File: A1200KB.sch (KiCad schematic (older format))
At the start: 118 parts, among them J1 Conn_01x32_Female, K1 ESC, K10 F9, K11 F10, K12 TILDE, K13 1, K14 2, K15 3, K16 4, K17 5, K18 6, K19 7, K2 F1, K20 8, K21 9, K22 0, K23 MINUS, K24 PLUS, K25 PIPE, K26 BS, K27 DEL, K28 HELP, K29 NUM_(, K3 F2, K30 NUM_), K31 NUM_DIV, K32 NUM_MULT, K33 TAB, K34 Q, K35 W, K36 E, K37 R, K38 T, K39 Y, K4 F3, K40 U, K41 I, K42 O, K43 P, K44 L.CURLY, K45 R.CURLY, K46 RETURN, K47 NUM_7, K48 NUM_8, K49 NUM_9, K5 F4, K50 NUM_MINUS, K51 CTRL, K52 CAPSLOCK, K53 A, K54 S, K55 D, K56 F, K57 G, K58 H, K59 J, K6 F5, K60 K, K61 L, K62 COLON, K63 \", K64 R.BLANK, K65 UP, K66 NUM_4, K67 NUM_5, K68 NUM_6, K69 NUM_PLUS, K7 F6, K70 L.SHIFT, K71 L.BLANK, K72 Z, K73 X, K74 C, K75 V, K76 B, K77 N, K78 M, K79 R.CROC, K8 F7, K80 L.CROC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

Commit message: Added some global netlist
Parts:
- removed U1, U?: STM32F401-DK, RetroBitLab:STM32F401-DK, symbol AmigaComponents:STM32F401-DK
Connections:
- net 27: now also K98.1 (COL)
- net 3: no longer K98.1 (COL)
- no-connect marks 0 -> 1
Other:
- note added: "From LOCAL Nets to GLOBAL Nets"
- moved on the sheet: K98

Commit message: Updated from AEBERBACH GitHub repo
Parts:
- removed H1, H11, H12, H13, H14, H15, H17, H18, H19, H2, H3, H5, H6, H7, H8, H9: MountingHole_Pad, MountingHole:MountingHole_3mm_Pad, symbol Mechanical:MountingHole_Pad
- removed K97: MENU, RetroBitLab:SW_Cherry_MX1A_1.00u_PCB_3d, symbol AmigaComponents:MX-1U-MX_Alps_Hybrids
- removed K98: SUPER, RetroBitLab:SW_Cherry_MX1A_1.00u_PCB_3d, symbol AmigaComponents:MX-1U-MX_Alps_Hybrids
- removed K99: SPACE 9U, RetroBitLab:SW_Cherry_MX1A_9u_PCB_3d, symbol AmigaComponents:MX-7U-MX_Alps_Hybrids
- J1: footprint RetroBitLab:MOLEX-FFC-1.25mm-RA-52044-3245 -> Connector_FFC-FPC:FFC-1.25mm-RA-5204403245
- K1, K13, K14, K15, K16, K17, K18, K19, K20, K21, K22, K23, K24, K25, K26, K29, K30, K31, K32, K34, K35, K36, K37, K38, K39, K40, K41, K42, K43, K44, K45, K47, K48, K49, K50, K53, K54, K55, K56, K57, K58, K59, K60, K61, K62, K63, K64, K65, K66, K67, K68, K69, K71, K72, K73, K74, K75, K76, K77, K78, K79, K80, K81, K83, K84, K85, K86, K87, K88, K96: footprint RetroBitLab:SW_Cherry_MX1A_1.00u_PCB_3d -> MX_Alps_Hybrid:MXOnly-1U-NoLED; symbol AmigaComponents:MX-1U-MX_Alps_Hybrids -> A1200KB-rescue:MX-1U-MX_Alps_Hybrids
- K10, K11, K2, K3, K4, K5, K51, K6, K7, K8, K9, K90, K91, K93, K94: footprint RetroBitLab:SW_Cherry_MX1A_1.25u_PCB_3d -> MX_Alps_Hybrid:MXOnly-1.25U-NoLED; symbol AmigaComponents:MX-1.25U-MX_Alps_Hybrids -> A1200KB-rescue:MX-1.25U-MX_Alps_Hybrids
- K12, K27, K28: footprint RetroBitLab:SW_Cherry_MX1A_1.50u_PCB_3d -> MX_Alps_Hybrid:MXOnly-1.5U-NoLED; symbol AmigaComponents:MX-1.5U-MX_Alps_Hybrids -> A1200KB-rescue:MX-1.5U-MX_Alps_Hybrids
- K33: footprint RetroBitLab:SW_Cherry_MX1A_1.00u_PCB_3d -> MX_Alps_Hybrid:MXOnly-2U-NoLED; symbol AmigaComponents:MX-2U-MX_Alps_Hybrids -> A1200KB-rescue:MX-2U-MX_Alps_Hybrids
- K46: footprint RetroBitLab:SW_Cherry_MX1A_ISOEnter_Rotated_PCB_3d -> MX_Alps_Hybrid:MXOnly-ISO; symbol AmigaComponents:MX-ISO-MX_Alps_Hybrids -> A1200KB-rescue:MX-ISO-MX_Alps_Hybrids
- K52: footprint RetroBitLab:MXOnly-1U -> MX_Alps_Hybrid:MXOnly-1U; symbol AmigaComponents:MX-1U-MX_Alps_Hybrids -> A1200KB-rescue:MX-1U-MX_Alps_Hybrids
- K70: footprint RetroBitLab:SW_Cherry_MX1A_1.75u_PCB_3d -> MX_Alps_Hybrid:MXOnly-1.75U-NoLED; symbol AmigaComponents:MX-1.75U-MX_Alps_Hybrids -> A1200KB-rescue:MX-1.75U-MX_Alps_Hybrids
- K82: footprint RetroBitLab:SW_Cherry_MX1A_2.75u_PCB_3d -> MX_Alps_Hybrid:MXOnly-2.75U-NoLED; symbol AmigaComponents:MX-2.75U-MX_Alps_Hybrids -> A1200KB-rescue:MX-2.75U-MX_Alps_Hybrids
- K89: footprint RetroBitLab:SW_Cherry_MX1A_2.00u_Vertical_PCB_3d -> MX_Alps_Hybrid:MXOnly-2U-NoLED; symbol AmigaComponents:MX-2U-MX_Alps_Hybrids -> A1200KB-rescue:MX-2U-MX_Alps_Hybrids
- K92: value SPACE 7U -> SPACE; footprint RetroBitLab:MXOnly-7U-NoSwitch -> MX_Alps_Hybrid:MXOnly-7U-NoLED; symbol AmigaComponents:MX-7U-MX_Alps_Hybrids -> A1200KB-rescue:MX-7U-MX_Alps_Hybrids
- K95: footprint RetroBitLab:SW_Cherry_MX1A_2.00u_PCB_3d -> MX_Alps_Hybrid:MXOnly-2U-NoLED; symbol AmigaComponents:MX-2U-MX_Alps_Hybrids -> A1200KB-rescue:MX-2U-MX_Alps_Hybrids
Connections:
- net labels removed: CAPSLOCK_LED, COL1, COL10, COL11, COL12, COL13, COL14, COL15, COL2, COL3, COL4, COL5, COL6, COL7, COL8, COL9, GND, ROW1, ROW10, ROW11, ROW12, ROW13, ROW2, ROW3, ROW4, ROW5, ROW6, ROW7, ROW8, ROW9, VCC_5V
- wire segments 659 -> 568
- no-connect marks 1 -> 0
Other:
- note removed: "From LOCAL Nets to GLOBAL Nets"

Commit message: Now has the AmigaComponents.lib dependancy
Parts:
- added H1, H11, H12, H13, H14, H15, H16, H17, H18, H19, H2, H3, H5, H6, H7, H8, H9: MountingHole_Pad, MountingHole:MountingHole_3mm_Pad, symbol Mechanical:MountingHole_Pad
- added K97: MENU, RetroBitLab:SW_Cherry_MX1A_1.00u_PCB_3d, symbol AmigaComponents:MX-1U-MX_Alps_Hybrids
- added K98: SUPER, RetroBitLab:SW_Cherry_MX1A_1.00u_PCB_3d, symbol AmigaComponents:MX-1U-MX_Alps_Hybrids
- added K99: SPACE 9U, RetroBitLab:SW_Cherry_MX1A_9u_PCB_3d, symbol AmigaComponents:MX-7U-MX_Alps_Hybrids
- added U1: STM32F401-DK, RetroBitLab:STM32F401-DK, symbol AmigaComponents:STM32F401-DK
- J1: footprint Connector_FFC-FPC:FFC-1.25mm-RA-5204403245 -> RetroBitLab:MOLEX-FFC-1.25mm-RA-52044-3245
- K1, K13, K14, K15, K16, K17, K18, K19, K20, K21, K22, K23, K24, K25, K26, K29, K30, K31, K32, K34, K35, K36, K37, K38, K39, K40, K41, K42, K43, K44, K45, K47, K48, K49, K50, K53, K54, K55, K56, K57, K58, K59, K60, K61, K62, K63, K64, K65, K66, K67, K68, K69, K71, K72, K73, K74, K75, K76, K77, K78, K79, K80, K81, K83, K84, K85, K86, K87, K88, K96: footprint MX_Alps_Hybrid:MXOnly-1U-NoLED -> RetroBitLab:SW_Cherry_MX1A_1.00u_PCB_3d; symbol A1200KB-rescue:MX-1U-MX_Alps_Hybrids -> AmigaComponents:MX-1U-MX_Alps_Hybrids
- K10, K11, K2, K3, K4, K5, K51, K6, K7, K8, K9, K90, K91, K93, K94: footprint MX_Alps_Hybrid:MXOnly-1.25U-NoLED -> RetroBitLab:SW_Cherry_MX1A_1.25u_PCB_3d; symbol A1200KB-rescue:MX-1.25U-MX_Alps_Hybrids -> AmigaComponents:MX-1.25U-MX_Alps_Hybrids
- K12, K27, K28: footprint MX_Alps_Hybrid:MXOnly-1.5U-NoLED -> RetroBitLab:SW_Cherry_MX1A_1.50u_PCB_3d; symbol A1200KB-rescue:MX-1.5U-MX_Alps_Hybrids -> AmigaComponents:MX-1.5U-MX_Alps_Hybrids
- K33: footprint MX_Alps_Hybrid:MXOnly-2U-NoLED -> RetroBitLab:SW_Cherry_MX1A_1.00u_PCB_3d; symbol A1200KB-rescue:MX-2U-MX_Alps_Hybrids -> AmigaComponents:MX-2U-MX_Alps_Hybrids
- K46: footprint MX_Alps_Hybrid:MXOnly-ISO -> RetroBitLab:SW_Cherry_MX1A_ISOEnter_PCB_3d; symbol A1200KB-rescue:MX-ISO-MX_Alps_Hybrids -> AmigaComponents:MX-ISO-MX_Alps_Hybrids
- K52: footprint MX_Alps_Hybrid:MXOnly-1U -> RetroBitLab:MXOnly-1U; symbol A1200KB-rescue:MX-1U-MX_Alps_Hybrids -> AmigaComponents:MX-1U-MX_Alps_Hybrids
- K70: footprint MX_Alps_Hybrid:MXOnly-1.75U-NoLED -> RetroBitLab:SW_Cherry_MX1A_1.75u_PCB_3d; symbol A1200KB-rescue:MX-1.75U-MX_Alps_Hybrids -> AmigaComponents:MX-1.75U-MX_Alps_Hybrids
- K82: footprint MX_Alps_Hybrid:MXOnly-2.75U-NoLED -> RetroBitLab:SW_Cherry_MX1A_2.75u_PCB_3d; symbol A1200KB-rescue:MX-2.75U-MX_Alps_Hybrids -> AmigaComponents:MX-2.75U-MX_Alps_Hybrids
- K89: footprint MX_Alps_Hybrid:MXOnly-2U-NoLED -> RetroBitLab:SW_Cherry_MX1A_2.00u_Vertical_PCB_3d; symbol A1200KB-rescue:MX-2U-MX_Alps_Hybrids -> AmigaComponents:MX-2U-MX_Alps_Hybrids
- K92: value SPACE -> SPACE 7U; footprint MX_Alps_Hybrid:MXOnly-7U-NoLED -> RetroBitLab:MXOnly-7U-NoSwitch; symbol A1200KB-rescue:MX-7U-MX_Alps_Hybrids -> AmigaComponents:MX-7U-MX_Alps_Hybrids
- K95: footprint MX_Alps_Hybrid:MXOnly-2U-NoLED -> RetroBitLab:SW_Cherry_MX1A_2.00u_PCB_3d; symbol A1200KB-rescue:MX-2U-MX_Alps_Hybrids -> AmigaComponents:MX-2U-MX_Alps_Hybrids
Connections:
- net labels added: GND
- wire segments 568 -> 588

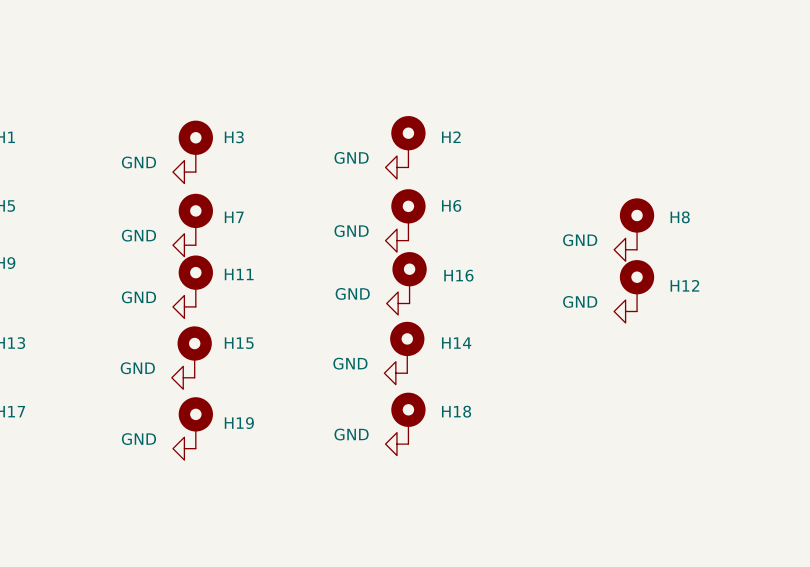
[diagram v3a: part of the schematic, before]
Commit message: The ISO Enter here, must have rotated Cherry MX switch by 180 degrees
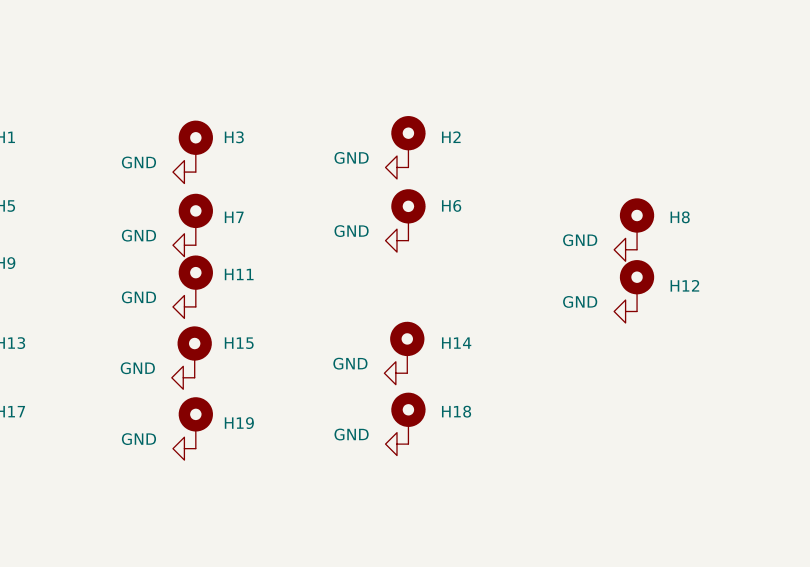
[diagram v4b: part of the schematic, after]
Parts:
- removed H16: MountingHole_Pad, MountingHole:MountingHole_3mm_Pad, symbol Mechanical:MountingHole_Pad
- K46: footprint RetroBitLab:SW_Cherry_MX1A_ISOEnter_PCB_3d -> RetroBitLab:SW_Cherry_MX1A_ISOEnter_Rotated_PCB_3d
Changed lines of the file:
@@
 Sheet 1 1
 Title "AMIGA 1200 KEYBOARD"
-Date ""
+Date "2022-01-14"
 Rev "1"
-Comp "ADAM EBERBACH"
-Comment1 ""
-Comment2 ""
+Comp "Original Concept by ADAM EBERBACH"
+Comment1 "Modified by RetroBit Lab"
+Comment2 "Gianluca Renzi"
 Comment3 ""
 Comment4 ""
@@
 F 0 "K46" H 14800 8039 60  0000 C CNN
 F 1 "RETURN" H 14800 7933 60  0000 C CNN
-F 2 "RetroBitLab:SW_Cherry_MX1A_ISOEnter_PCB_3d" H 14800 7933 60  0001 C CNN
+F 2 "RetroBitLab:SW_Cherry_MX1A_ISOEnter_Rotated_PCB_3d" H 14800 7933 60  0001 C CNN
 F 3 "" H 14800 7700 60  0000 C CNN
 	1    14800 7700
@@
 $EndComp
 $Comp
-L Mechanical:MountingHole_Pad H16
-U 1 1 6238099B
-P 16415 12725
-F 0 "H16" H 16560 12745 50  0000 L CNN
-F 1 "MountingHole_Pad" H 16540 12725 50  0001 L CNN
-F 2 "MountingHole:MountingHole_3mm_Pad" H 16415 12725 50  0001 C CNN
-F 3 "~" H 16415 12725 50  0001 C CNN
-	1    16415 12725
-	1    0    0    -1
-$EndComp
-$Comp
 L power:GND #PWR0101
 U 1 1 623E1EAF
@@
 	0    1    1    0
 $EndComp
-$Comp
-L power:GND #PWR0117
-U 1 1 623E59EB
-P 16415 12825
-F 0 "#PWR0117" H 16415 12575 50  0001 C CNN
-F 1 "GND" V 16375 12655 50  0000 R CNN
-F 2 "" H 16415 12825 50  0001 C CNN
-F 3 "" H 16415 12825 50  0001 C CNN
-	1    16415 12825
-	0    1    1    0
-$EndComp

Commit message: Added MCU controller sheet page
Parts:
- added U?: STM32F401-DK, RetroBitLab:STM32F401-DK, symbol AmigaComponents:STM32F401-DK
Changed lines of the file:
@@
 $Descr A2 23386 16535
 encoding utf-8
-Sheet 1 1
+Sheet 1 2
 Title "AMIGA 1200 KEYBOARD"
 Date "2022-01-14"
@@
 	0    1    1    0
 $EndComp
+$Sheet
+S 0    16885 23385 7255
+U 61EC24E4
+F0 " MCU_Controller" 50
+F1 "MCU_Controller.sch" 50
+$EndSheet
 $Comp
 L AmigaComponents:STM32F401-DK U1
@@
 	1    0    0    -1
 $EndComp
+$Comp
+L AmigaComponents:STM32F401-DK U?
+U 1 1 61F4DD88
+P 10325 13545
+F 0 "U?" H 11460 13600 50  0000 L CNN
+F 1 "STM32F401-DK" H 11460 13500 50  0000 L CNN
+F 2 "RetroBitLab:STM32F401-DK" H 10575 14195 50  0001 C CNN
+F 3 "" H 10575 14195 50  0001 C CNN
+	1    10325 13545
+	1    0    0    -1
+$EndComp
